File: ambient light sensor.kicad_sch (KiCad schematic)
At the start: 5 parts, among them Q3 TEPT5700

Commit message: Major Changes
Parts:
- renumbered C44 to C45, R28 to R30, R29 to R31
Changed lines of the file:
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@@
 	(title_block
 		(title "Ambient Light Sensor")
-		(date "2026-02-09")
+		(date "2026-02-13")
 		(rev "v0.0")
 		(company "TJ71PL")
@@
 		(dnp no)
 		(fields_autoplaced yes)
-		(property "Reference" "R28"
+		(property "Reference" "R30"
 			(at 148.59 86.3599 0)
 			(effects
@@
 			(project "Precision Clock"
 				(path "/c9a8ff63-a0d1-4125-9dd1-40fb53daf536/f0b87a8b-19e9-4032-a495-3b751ae7ab11"
-					(reference "R28")
+					(reference "R30")
 					(unit 1)
 				)
@@
 		(dnp no)
 		(fields_autoplaced yes)
-		(property "Reference" "#PWR0118"
+		(property "Reference" "#PWR0125"
 			(at 146.05 119.38 0)
 			(effects
@@
 			(project ""
 				(path "/c9a8ff63-a0d1-4125-9dd1-40fb53daf536/f0b87a8b-19e9-4032-a495-3b751ae7ab11"
-					(reference "#PWR0118")
+					(reference "#PWR0125")
 					(unit 1)
 				)
@@
 		(dnp no)
 		(fields_autoplaced yes)
-		(property "Reference" "C44"
+		(property "Reference" "C45"
 			(at 137.16 86.3599 0)
 			(effects
@@
 			(project "Precision Clock"
 				(path "/c9a8ff63-a0d1-4125-9dd1-40fb53daf536/f0b87a8b-19e9-4032-a495-3b751ae7ab11"
-					(reference "C44")
+					(reference "C45")
 					(unit 1)
 				)
@@
 		(dnp no)
 		(fields_autoplaced yes)
-		(property "Reference" "#PWR0117"
+		(property "Reference" "#PWR0124"
 			(at 146.05 82.55 0)
 			(effects
@@
 			(project "Precision Clock"
 				(path "/c9a8ff63-a0d1-4125-9dd1-40fb53daf536/f0b87a8b-19e9-4032-a495-3b751ae7ab11"
-					(reference "#PWR0117")
+					(reference "#PWR0124")
 					(unit 1)
 				)
@@
 		(dnp no)
 		(fields_autoplaced yes)
-		(property "Reference" "#PWR0116"
+		(property "Reference" "#PWR0123"
 			(at 133.35 100.33 0)
 			(effects
@@
 			(project ""
 				(path "/c9a8ff63-a0d1-4125-9dd1-40fb53daf536/f0b87a8b-19e9-4032-a495-3b751ae7ab11"
-					(reference "#PWR0116")
+					(reference "#PWR0123")
 					(unit 1)
 				)
@@
 		(dnp no)
 		(fields_autoplaced yes)
-		(property "Reference" "R29"
+		(property "Reference" "R31"
 			(at 158.75 88.9 90)
 			(effects
@@
 			(project "Precision Clock"
 				(path "/c9a8ff63-a0d1-4125-9dd1-40fb53daf536/f0b87a8b-19e9-4032-a495-3b751ae7ab11"
-					(reference "R29")
+					(reference "R31")
 					(unit 1)
 				)

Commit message: Verification
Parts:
- renumbered C45 to C5, Q3 to Q4, R30 to R6, R31 to R7, TP16 to TP3
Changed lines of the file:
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@@
 	(title_block
 		(title "Ambient Light Sensor")
-		(date "2026-02-13")
+		(date "2026-02-25")
 		(rev "v0.0")
 		(company "TJ71PL")
-		(comment 1 "天計")
 		(comment 4 "Final verification complete")
 	)
@@
 		(on_board yes)
 		(dnp no)
-		(property "Reference" "Q3"
+		(property "Reference" "Q4"
 			(at 148.59 101.6 0)
 			(effects
@@
 			(project ""
 				(path "/c9a8ff63-a0d1-4125-9dd1-40fb53daf536/f0b87a8b-19e9-4032-a495-3b751ae7ab11"
-					(reference "Q3")
+					(reference "Q4")
 					(unit 1)
 				)
@@
 		(dnp no)
 		(fields_autoplaced yes)
-		(property "Reference" "TP16"
+		(property "Reference" "TP3"
 			(at 170.18 88.1379 0)
 			(effects
@@
 			(project ""
 				(path "/c9a8ff63-a0d1-4125-9dd1-40fb53daf536/f0b87a8b-19e9-4032-a495-3b751ae7ab11"
-					(reference "TP16")
+					(reference "TP3")
 					(unit 1)
 				)
@@
 		(dnp no)
 		(fields_autoplaced yes)
-		(property "Reference" "R30"
+		(property "Reference" "R6"
 			(at 148.59 86.3599 0)
 			(effects
@@
 			(project "Precision Clock"
 				(path "/c9a8ff63-a0d1-4125-9dd1-40fb53daf536/f0b87a8b-19e9-4032-a495-3b751ae7ab11"
-					(reference "R30")
+					(reference "R6")
 					(unit 1)
 				)
@@
 		(dnp no)
 		(fields_autoplaced yes)
-		(property "Reference" "#PWR0125"
+		(property "Reference" "#PWR0123"
 			(at 146.05 119.38 0)
 			(effects
@@
 			(project ""
 				(path "/c9a8ff63-a0d1-4125-9dd1-40fb53daf536/f0b87a8b-19e9-4032-a495-3b751ae7ab11"
-					(reference "#PWR0125")
+					(reference "#PWR0123")
 					(unit 1)
 				)
@@
 		(dnp no)
 		(fields_autoplaced yes)
-		(property "Reference" "C45"
+		(property "Reference" "C5"
 			(at 137.16 86.3599 0)
 			(effects
@@
 			(project "Precision Clock"
 				(path "/c9a8ff63-a0d1-4125-9dd1-40fb53daf536/f0b87a8b-19e9-4032-a495-3b751ae7ab11"
-					(reference "C45")
+					(reference "C5")
 					(unit 1)
 				)
@@
 		(dnp no)
 		(fields_autoplaced yes)
-		(property "Reference" "#PWR0124"
+		(property "Reference" "#PWR0122"
 			(at 146.05 82.55 0)
 			(effects
@@
 			(project "Precision Clock"
 				(path "/c9a8ff63-a0d1-4125-9dd1-40fb53daf536/f0b87a8b-19e9-4032-a495-3b751ae7ab11"
-					(reference "#PWR0124")
+					(reference "#PWR0122")
 					(unit 1)
 				)
@@
 		(dnp no)
 		(fields_autoplaced yes)
-		(property "Reference" "#PWR0123"
+		(property "Reference" "#PWR0121"
 			(at 133.35 100.33 0)
 			(effects
@@
 			(project ""
 				(path "/c9a8ff63-a0d1-4125-9dd1-40fb53daf536/f0b87a8b-19e9-4032-a495-3b751ae7ab11"
-					(reference "#PWR0123")
+					(reference "#PWR0121")
 					(unit 1)
 				)
@@
 		(dnp no)
 		(fields_autoplaced yes)
-		(property "Reference" "R31"
+		(property "Reference" "R7"
 			(at 158.75 88.9 90)
 			(effects
@@
 			(project "Precision Clock"
 				(path "/c9a8ff63-a0d1-4125-9dd1-40fb53daf536/f0b87a8b-19e9-4032-a495-3b751ae7ab11"
-					(reference "R31")
+					(reference "R7")
 					(unit 1)
 				)

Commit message: Encoder placement
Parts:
- renumbered C5 to C6, R6 to R9
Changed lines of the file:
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@@
 		(dnp no)
 		(fields_autoplaced yes)
-		(property "Reference" "R6"
+		(property "Reference" "R9"
 			(at 148.59 86.3599 0)
 			(effects
@@
 			(project "Precision Clock"
 				(path "/c9a8ff63-a0d1-4125-9dd1-40fb53daf536/f0b87a8b-19e9-4032-a495-3b751ae7ab11"
-					(reference "R6")
+					(reference "R9")
 					(unit 1)
 				)
@@
 		(dnp no)
 		(fields_autoplaced yes)
-		(property "Reference" "C5"
+		(property "Reference" "C6"
 			(at 137.16 86.3599 0)
 			(effects
@@
 			(project "Precision Clock"
 				(path "/c9a8ff63-a0d1-4125-9dd1-40fb53daf536/f0b87a8b-19e9-4032-a495-3b751ae7ab11"
-					(reference "C5")
+					(reference "C6")
 					(unit 1)
 				)

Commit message: Minor changes
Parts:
- renumbered C6 to C5, R9 to R11, R7 to R12
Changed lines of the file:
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@@
 		(dnp no)
 		(fields_autoplaced yes)
-		(property "Reference" "R9"
+		(property "Reference" "R11"
 			(at 148.59 86.3599 0)
 			(effects
@@
 			(project "Precision Clock"
 				(path "/c9a8ff63-a0d1-4125-9dd1-40fb53daf536/f0b87a8b-19e9-4032-a495-3b751ae7ab11"
-					(reference "R9")
+					(reference "R11")
 					(unit 1)
 				)
@@
 		(dnp no)
 		(fields_autoplaced yes)
-		(property "Reference" "C6"
+		(property "Reference" "C5"
 			(at 137.16 86.3599 0)
 			(effects
@@
 			(project "Precision Clock"
 				(path "/c9a8ff63-a0d1-4125-9dd1-40fb53daf536/f0b87a8b-19e9-4032-a495-3b751ae7ab11"
-					(reference "C6")
+					(reference "C5")
 					(unit 1)
 				)
@@
 		(dnp no)
 		(fields_autoplaced yes)
-		(property "Reference" "R7"
+		(property "Reference" "R12"
 			(at 158.75 88.9 90)
 			(effects
@@
 			(project "Precision Clock"
 				(path "/c9a8ff63-a0d1-4125-9dd1-40fb53daf536/f0b87a8b-19e9-4032-a495-3b751ae7ab11"
-					(reference "R7")
-					(unit 1)
-				)
+					(reference "R12")
+					(unit 1)
+				)

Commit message: Production files preparation
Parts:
- C5: LCSC (none) -> C1525
- Q4: LCSC 782-TEPT5700 -> (none); Mouser (none) -> 782-TEPT5700; now left out of the parts list
- R13: renamed from R11; LCSC (none) -> C60489
- R15: renamed from R12; LCSC (none) -> C276273
- TP3: now left out of the parts list
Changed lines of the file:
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@@
 		(unit 1)
 		(exclude_from_sim no)
-		(in_bom yes)
+		(in_bom no)
 		(on_board yes)
 		(dnp no)
@@
 			)
 		)
-		(property "LCSC" "782-TEPT5700"
+		(property "Mouser" "782-TEPT5700"
 			(at 148.59 106.4134 0)
 			(effects
@@
 		(unit 1)
 		(exclude_from_sim no)
-		(in_bom yes)
+		(in_bom no)
 		(on_board yes)
 		(dnp no)
@@
 		(dnp no)
 		(fields_autoplaced yes)
-		(property "Reference" "R11"
+		(property "Reference" "R13"
 			(at 148.59 86.3599 0)
 			(effects
@@
 			)
 		)
+		(property "LCSC" "C60489"
+			(at 146.05 87.63 0)
+			(effects
+				(font
+					(size 1.27 1.27)
+				)
+				(hide yes)
+			)
+		)
 		(pin "1"
 		)
@@
 			(project "Precision Clock"
 				(path "/c9a8ff63-a0d1-4125-9dd1-40fb53daf536/f0b87a8b-19e9-4032-a495-3b751ae7ab11"
-					(reference "R11")
+					(reference "R13")
 					(unit 1)
 				)
@@
 			)
 		)
+		(property "LCSC" "C1525"
+			(at 133.35 87.63 0)
+			(effects
+				(font
+					(size 1.27 1.27)
+				)
+				(hide yes)
+			)
+		)
 		(pin "2"
 		)
@@
 		(dnp no)
 		(fields_autoplaced yes)
-		(property "Reference" "R12"
+		(property "Reference" "R15"
 			(at 158.75 88.9 90)
 			(effects
@@
 			)
 		)
+		(property "LCSC" "C276273"
+			(at 158.75 95.25 0)
+			(effects
+				(font
+					(size 1.27 1.27)
+				)
+				(hide yes)
+			)
+		)
 		(pin "1"
 		)
@@
 			(project "Precision Clock"
 				(path "/c9a8ff63-a0d1-4125-9dd1-40fb53daf536/f0b87a8b-19e9-4032-a495-3b751ae7ab11"
-					(reference "R12")
-					(unit 1)
-				)
+					(reference "R15")
+					(unit 1)
+				)

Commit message: In Production
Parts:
- Q4: LCSC (none) -> 782-TEPT5700
- renumbered R13 to R14
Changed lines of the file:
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@@
+			)
+		)
+		(property "LCSC" "782-TEPT5700"
+			(at 143.51 104.14 0)
+			(effects
+				(font
+					(size 1.27 1.27)
+				)
+				(hide yes)
 			)
 		)
@@
 		(dnp no)
 		(fields_autoplaced yes)
-		(property "Reference" "R13"
+		(property "Reference" "R14"
 			(at 148.59 86.3599 0)
 			(effects
@@
 			(project "Precision Clock"
 				(path "/c9a8ff63-a0d1-4125-9dd1-40fb53daf536/f0b87a8b-19e9-4032-a495-3b751ae7ab11"
-					(reference "R13")
+					(reference "R14")
 					(unit 1)
 				)

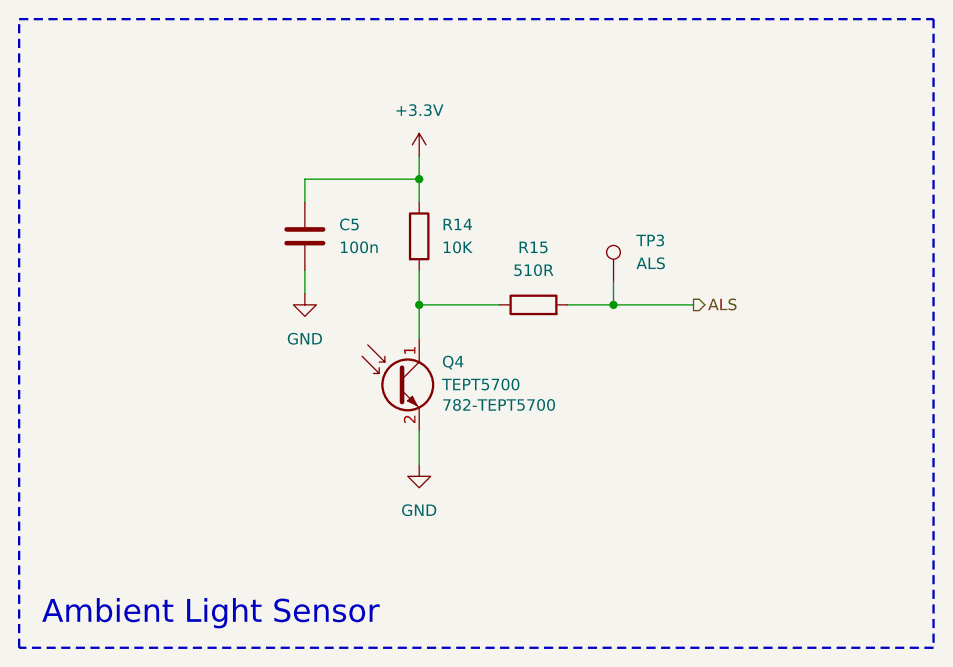
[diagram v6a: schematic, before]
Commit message: Push Button Replacement
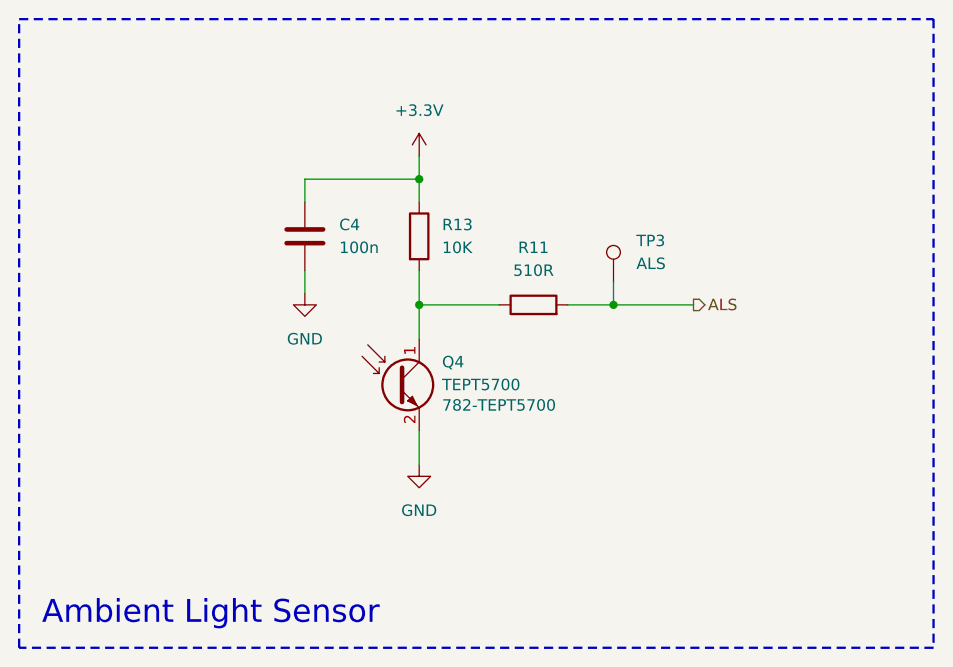
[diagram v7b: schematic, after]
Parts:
- renumbered C5 to C4, R15 to R11, R14 to R13
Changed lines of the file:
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@@
 	(title_block
 		(title "Ambient Light Sensor")
-		(date "2026-02-25")
+		(date "2026-03-01")
 		(rev "v0.0")
 		(company "TJ71PL")
@@
 		(dnp no)
 		(fields_autoplaced yes)
-		(property "Reference" "R14"
+		(property "Reference" "R13"
 			(at 148.59 86.3599 0)
 			(effects
@@
 			(project "Precision Clock"
 				(path "/c9a8ff63-a0d1-4125-9dd1-40fb53daf536/f0b87a8b-19e9-4032-a495-3b751ae7ab11"
-					(reference "R14")
+					(reference "R13")
 					(unit 1)
 				)
@@
 		(dnp no)
 		(fields_autoplaced yes)
-		(property "Reference" "C5"
+		(property "Reference" "C4"
 			(at 137.16 86.3599 0)
 			(effects
@@
 			(project "Precision Clock"
 				(path "/c9a8ff63-a0d1-4125-9dd1-40fb53daf536/f0b87a8b-19e9-4032-a495-3b751ae7ab11"
-					(reference "C5")
+					(reference "C4")
 					(unit 1)
 				)
@@
 		(dnp no)
 		(fields_autoplaced yes)
-		(property "Reference" "R15"
+		(property "Reference" "R11"
 			(at 158.75 88.9 90)
 			(effects
@@
 			(project "Precision Clock"
 				(path "/c9a8ff63-a0d1-4125-9dd1-40fb53daf536/f0b87a8b-19e9-4032-a495-3b751ae7ab11"
-					(reference "R15")
+					(reference "R11")
 					(unit 1)
 				)
